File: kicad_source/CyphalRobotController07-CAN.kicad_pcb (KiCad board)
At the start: 2 copper layers, 140 x 70 mm, 178 parts, among them J1 BM04B-SRSS-TB, J10 x, J11 PowerPole, J12 Conn_01x02, J13 Conn_01x02, J14 Conn_01x02, J15 PinHeader_1x04, J16 PinHeader_1x04, J17 PinHeader_1x05, J18 Conn_01x02, J19 S6B-XH-A, J2 RASPBERRYPI_PICO, J20 S6B-XH-A, J3 BM04B-SRSS-TB, J4 B3B-PH-SM4-TB, J5 BM04B-GHS-TBT, J6 BM04B-GHS-TBT, J7 x, J8 x, J9 x, Q1 2N7002, Q2 IPD90P03P4L- 04, SW1 PTS636 SM43 SMTR LFS, U1 24LC64-I/SN, U10 ADS1015IDGS, U11 OPA2374AIDCN, U12 INA226, U13 IFX91041EFJ, U14 ITS4200S-ME-P, U15 ITS4200S-ME-P, U16 BNO085, U17 SN74LVC2T45DCUR, U18 SN74LVC2T45DCUR, U2 MCP2515-I/SO, U3 SN65HVD232, U4 74xx08, U5 IFX007T, U6 IFX007T, U7 IFX007T, U8 IFX007T, U9 OPA2374AIDCN, Y1 RH100-16.000-16-3030-EXT-TR, Y2 DNI

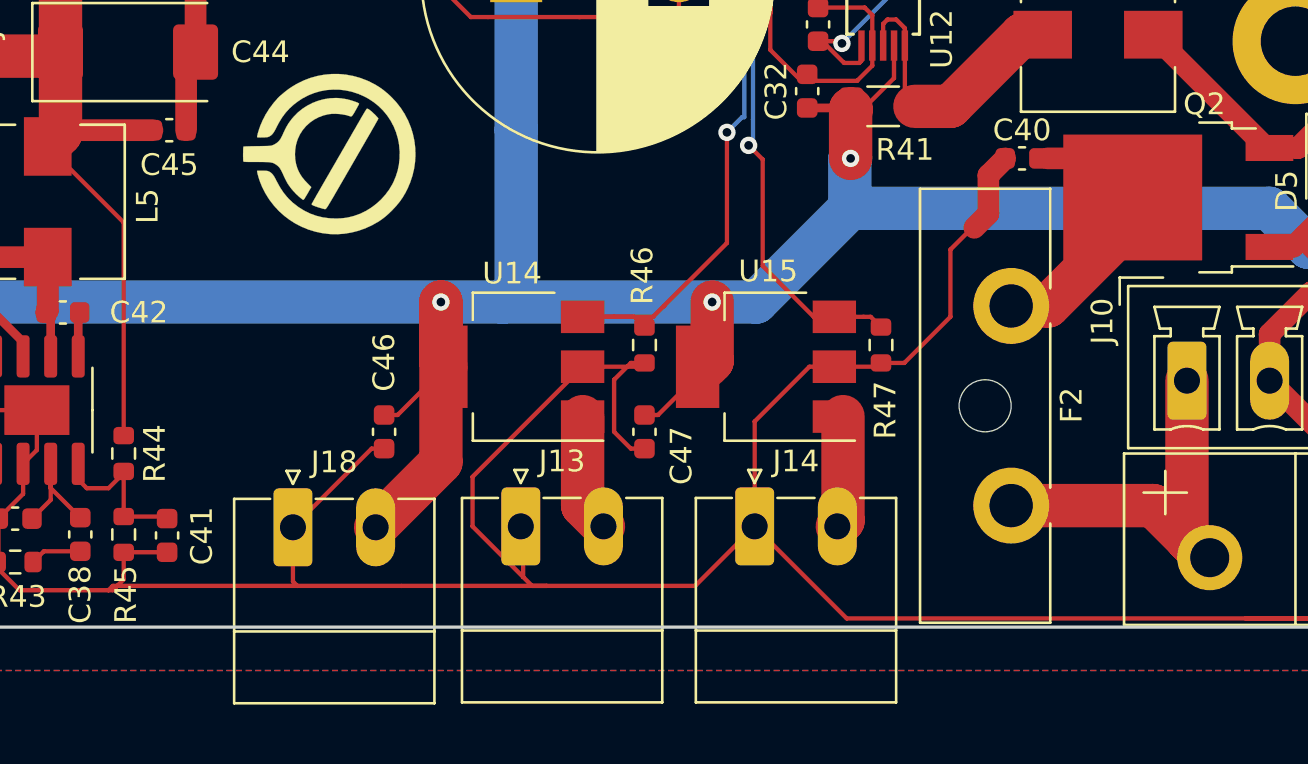
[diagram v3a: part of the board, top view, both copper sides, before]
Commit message: added tvs diode on input
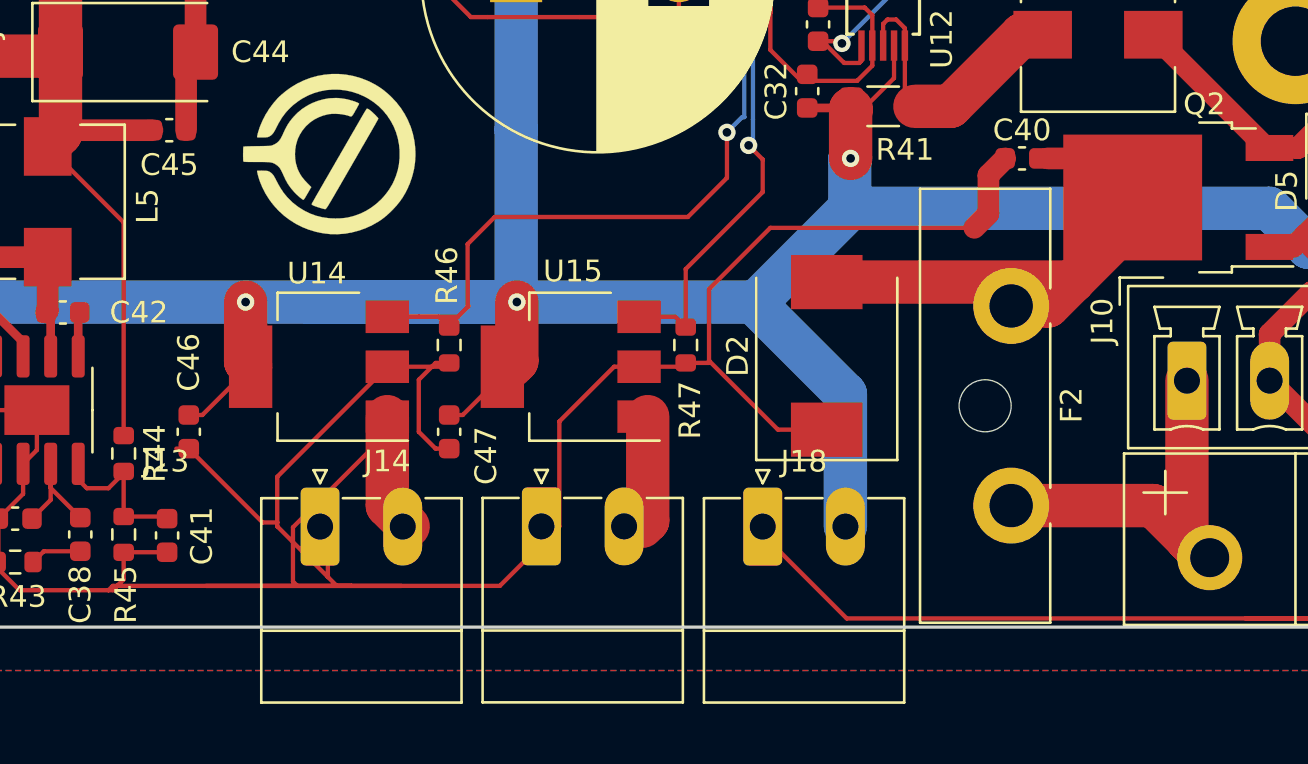
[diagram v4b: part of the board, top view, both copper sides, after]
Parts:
- added D2: SMCJ40A, Diode_SMD:D_SMC, F.Cu at (99.4, 113.5)
- moved J18 21.7 mm to (96.5, 121.4)
- moved J14 9.83 mm to (86.2, 121.4)
- moved J13 9.25 mm to (76.0, 121.4)
- moved C46 9.00 mm to (70.0, 117.0)
- moved C47 9.00 mm to (82.0, 117.0)
- moved R46 9.00 mm to (82.0, 113.0)
- moved R47 9.00 mm to (92.9, 113.0)
- moved U14 9.00 mm to (76.0, 114.0)
- moved U15 9.00 mm to (87.6, 114.0)
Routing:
- net GND: track 1078.6 -> 1100.0 mm
- net /VoltageRegulator/+BATT_Q: track 13.6 -> 25.1 mm
- net OUTPUT0: track 46.4 -> 55.4 mm
- net +BATT: track 345.3 -> 353.9 mm

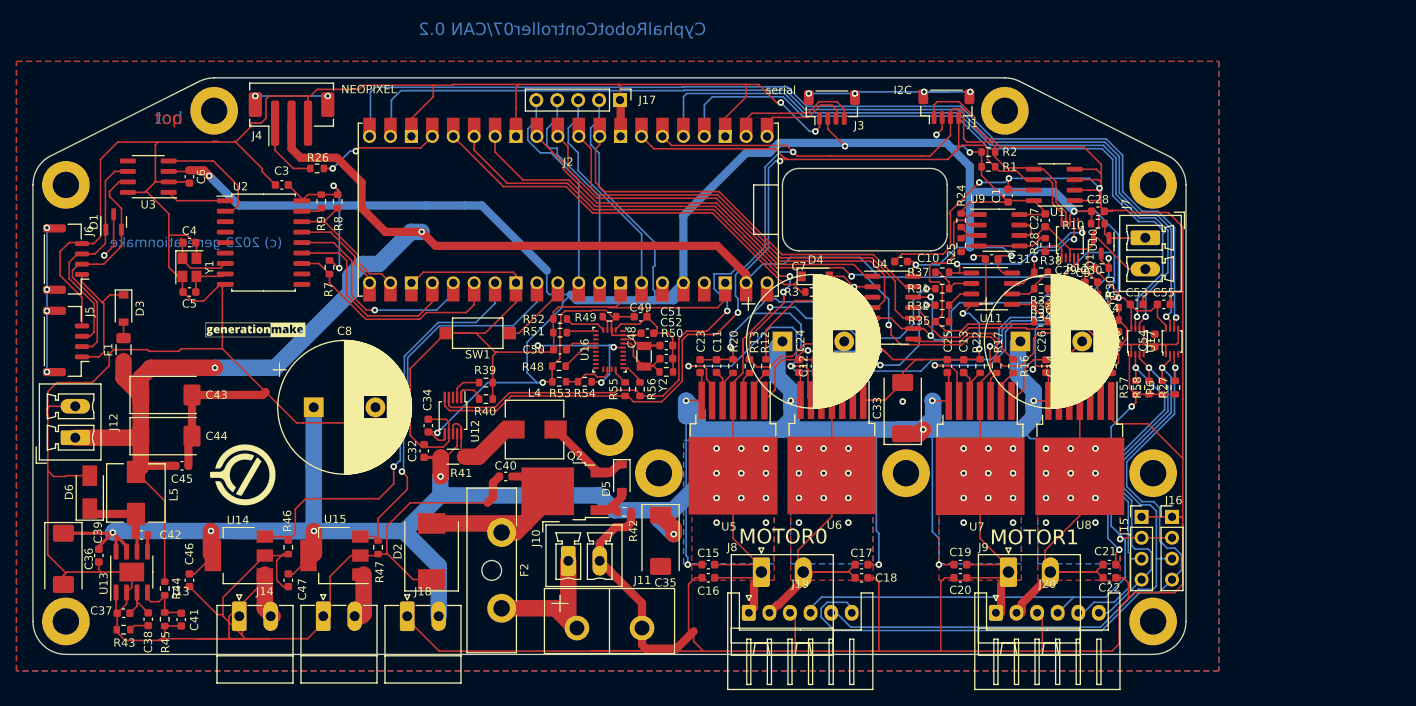
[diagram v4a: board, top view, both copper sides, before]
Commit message: replaced tantal with electrolytic capacitors
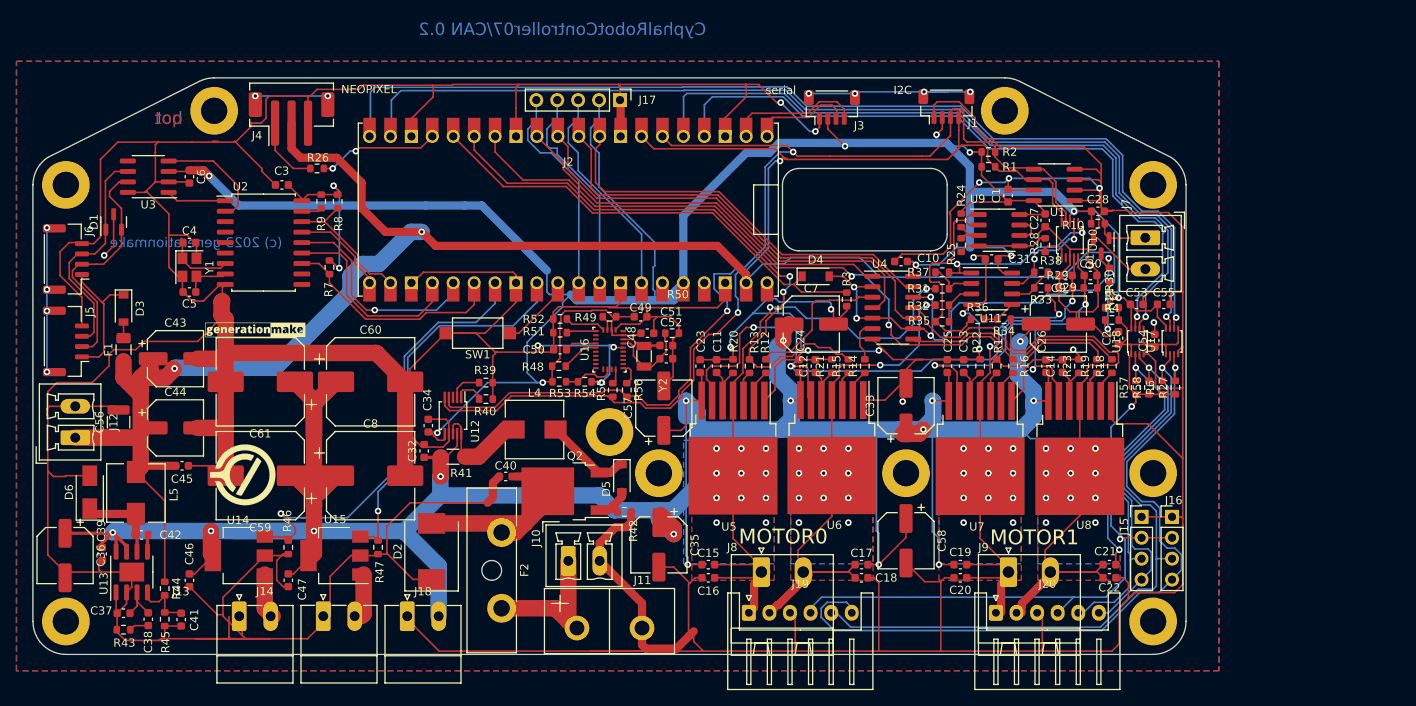
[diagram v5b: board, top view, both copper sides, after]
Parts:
- added C56: 100uF 6.3V, Capacitor_SMD:C_1210_3225Metric, F.Cu at (61.4, 97.8)
- added C57: 100uF 50V, Capacitor_SMD:CP_Elec_6.3x7.7, F.Cu at (127.6, 96.1)
- added C58: 100uF 50V, Capacitor_SMD:CP_Elec_6.3x7.7, F.Cu at (157.0, 112.2)
- added C59: 330uF 50V, Capacitor_SMD:CP_Elec_10x12.5, F.Cu at (78.6, 104.3)
- added C60: 330uF 50V, Capacitor_SMD:CP_Elec_10x12.5, F.Cu at (92.0, 92.9)
- added C61: 330uF 50V, Capacitor_SMD:CP_Elec_10x12.5, F.Cu at (78.6, 92.9)
- C33, C35, C36: value 47uF 50V -> 100uF 50V; footprint Capacitor_Tantalum_SMD:CP_EIA-7343-15_Kemet-W -> Capacitor_SMD:CP_Elec_6.3x7.7
- C43, C44: value 330uF 6.3V -> 680uF 6.3V; footprint Capacitor_Tantalum_SMD:CP_EIA-7343-15_Kemet-W -> Capacitor_SMD:CP_Elec_6.3x7.7
- C7, C9: value 1000uF 50V -> 100uF 50V; footprint Capacitor_THT:CP_Radial_D16.0mm_P7.50mm -> Capacitor_SMD:CP_Elec_6.3x7.7
- C8: value 1000uF 50V -> 330uF 50V; footprint Capacitor_THT:CP_Radial_D16.0mm_P7.50mm -> Capacitor_SMD:CP_Elec_10x12.5
- moved C8 10.8 mm to (92.0, 104.3)
- moved R36 7.71 mm to (165.7, 85.3)
- moved C9 5.07 mm to (175.5, 85.9)
- moved R34 4.81 mm to (168.9, 85.3)
- moved R50 4.75 mm to (128.6, 87.0)
- moved C43 4.54 mm to (68.3, 90.1)
- moved R3 4.30 mm to (149.8, 82.9), turned to -90 degrees
- moved C7 4.08 mm to (145.5, 85.9)
- moved R56 1.60 mm to (123.1, 93.9)
- moved R55 1.50 mm to (121.4, 93.9)
- moved C44 1.49 mm to (68.3, 98.5)
- moved R11 1.20 mm to (181.7, 79.9), turned to 90 degrees
- moved C30 0.81 mm to (179.4, 80.0)
- moved R30 0.81 mm to (179.4, 81.5)
- moved C29 0.80 mm to (176.4, 80.0), turned to 180 degrees
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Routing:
- net GND: track 1100.0 -> 1155.7 mm, vias 17 -> 19
- net +BATT: track 353.9 -> 392.6 mm, vias 14 -> 16
- net /Measurement/VREF: track 34.1 -> 26.7 mm
- net OUT4: track 63.8 -> 69.7 mm
- net EM_STOP_D: track 52.0 -> 57.0 mm
- net +5V: track 213.6 -> 216.9 mm
- net INH34: track 96.2 -> 92.9 mm
- net OUTPUT0: track 55.4 -> 58.5 mm
- net IS12: track 78.2 -> 75.3 mm
- net +3.3V: track 359.5 -> 356.9 mm
- net OUT1: track 82.6 -> 81.0 mm
- net /BNO085/CLKSEL1: track 8.83 -> 10.2 mm
- net /Measurement/OUT4R: track 5.42 -> 4.09 mm
- net I2C_SCL: track 132.6 -> 133.5 mm
- net /MotorDriver/PWM4_U: track 29.2 -> 29.9 mm
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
